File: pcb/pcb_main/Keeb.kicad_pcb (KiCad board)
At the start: 2 copper layers, 97.6 x 69.7 mm, 91 parts, among them J1 TRRS_SJ1-42514, Q1 PZT3906, SW1 SW_RST, SW2 SW_SPDT, U1 ATMEGA32U4, U2 SN74HC138D‎, U3 SN74HC251, U4 MCP73833, U5 LM8364-2.2, U6 LTC3525-5, X1 XTAL_GND

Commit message: Completed first revision of module1, started on module 2
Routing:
- net GND: track 93.7 -> 129.4 mm, vias 45 -> 35
- removed copper zone on F.Cu, net GND

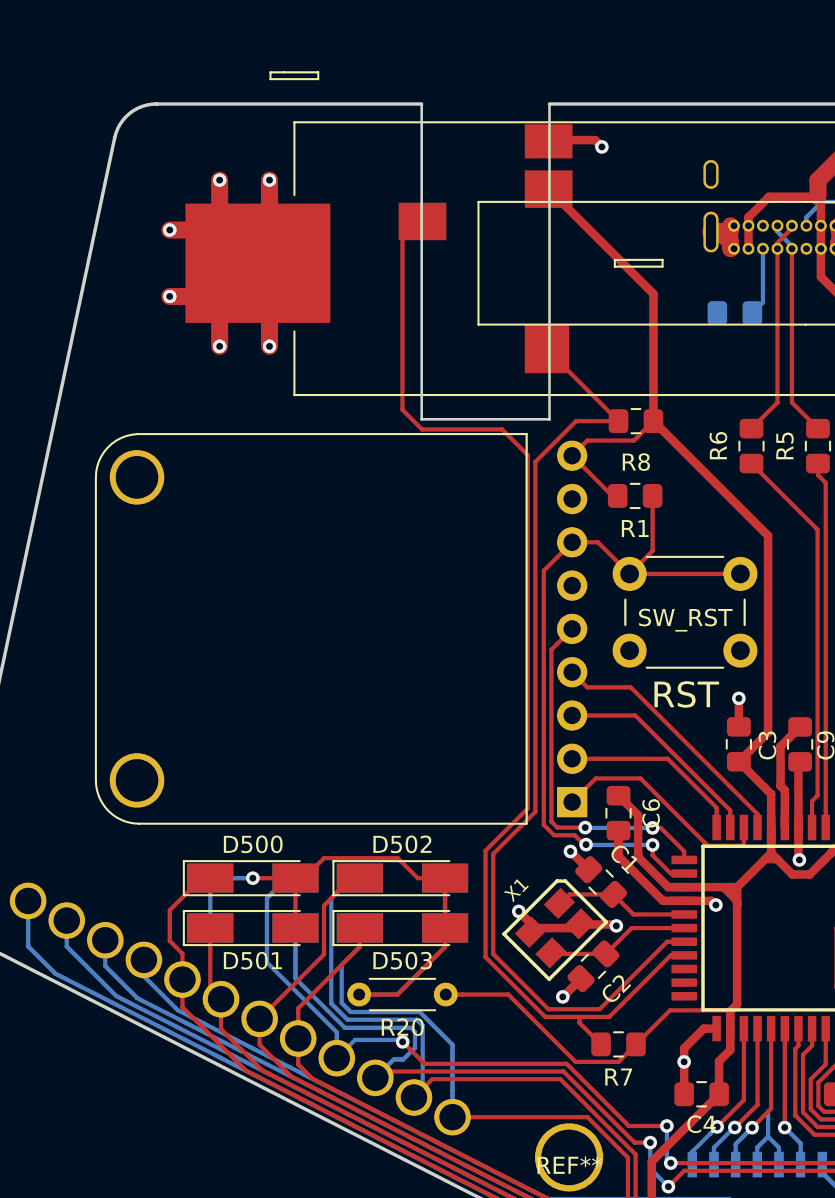
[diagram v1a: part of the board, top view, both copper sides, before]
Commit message: Rev 1 of module 2 & updated all-in-one cad drawing
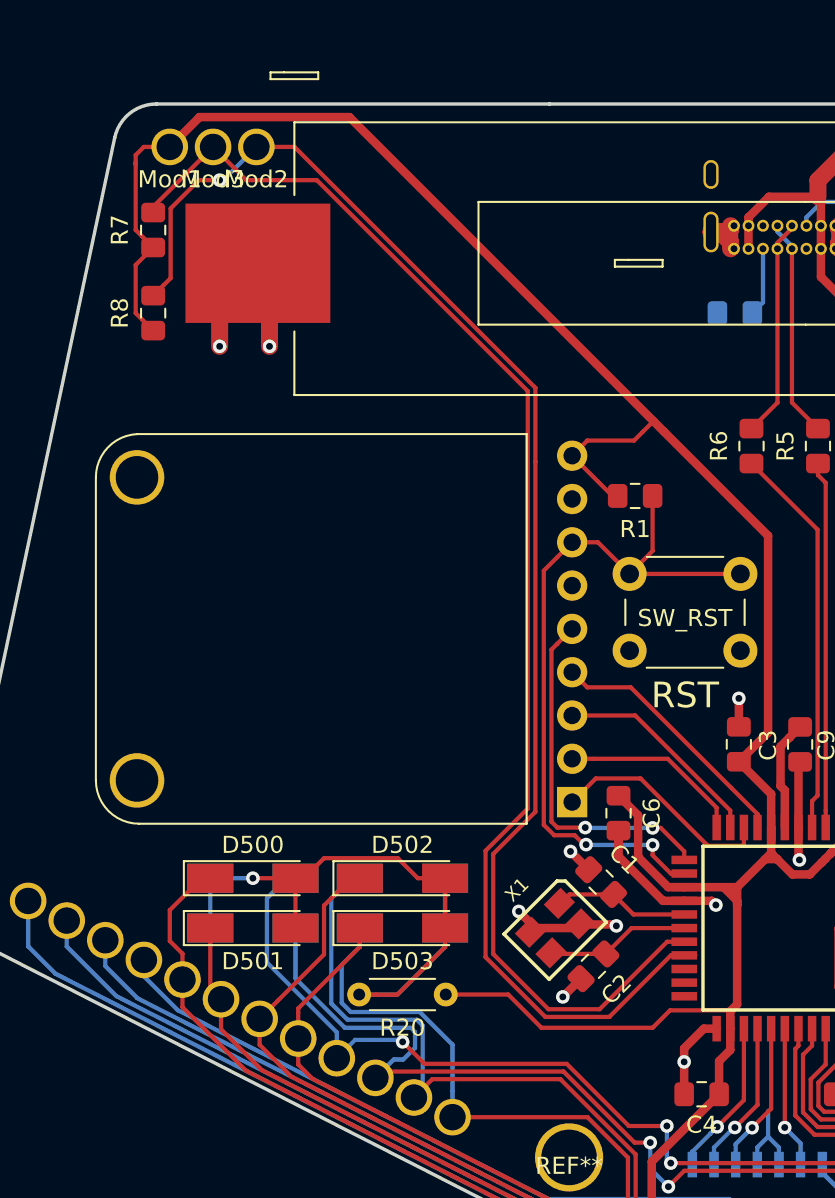
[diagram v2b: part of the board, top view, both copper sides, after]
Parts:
- removed J1: TRRS_SJ1-42514, SVastaCustomParts:3.5mm_Cut_out
- added Mod1: Conn_01x01_Male, SVastaCustomParts:Mill-Max_Pin_Socket_7305-0-15-15-47-27-10-0, F.Cu at (385.5, 162.0)
- added Mod2: Conn_01x01_Male, SVastaCustomParts:Mill-Max_Pin_Socket_7305-0-15-15-47-27-10-0, F.Cu at (390.5, 162.0)
- added Mod3: Conn_01x01_Male, SVastaCustomParts:Mill-Max_Pin_Socket_7305-0-15-15-47-27-10-0, F.Cu at (388.0, 162.0)
- moved R7 55.0 mm to (384.5, 166.9), turned to 270 degrees
- moved R8 29.0 mm to (384.5, 171.8), turned to 270 degrees
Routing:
- net VCC: track 213.7 -> 247.1 mm
- net SCL: track 55.1 -> 82.7 mm, vias 0 -> 1
- net GND: track 129.4 -> 113.4 mm, vias 35 -> 30
- net SDA: track 67.9 -> 79.2 mm
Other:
- outline, holes or cut-outs redrawn

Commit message: Updated connection method on main pcb
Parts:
- removed ColL0, ColL1, ColL2, ColL3, ColL4, ColL5, ColL6, ColL7, ColR0, ColR1, ColR2, ColR3, ColR4, ColR5, ColR6, ColR7, Mod1, Mod2, Mod3, Row0, Row1, Row2, Row3, Row4, Row5, Row6, Row7: Conn_01x01_Male, SVastaCustomParts:Mill-Max_Pin_Socket_7305-0-15-15-47-27-10-0
- removed REF** (x2): MountingHole_Imperial4-40_FreeFit, SVastaCustomParts:MountingHole_Imperial4-40_FreeFit
- added J101: Conn_02x10_Counter_Clockwise, SVastaCustomParts:Backplane_Connector_Hirose_PCN_20pos_Plug, F.Cu at (448.8, 206.9)
- added J102: Conn_02x10_Counter_Clockwise, SVastaCustomParts:Backplane_Connector_Hirose_PCN_20pos_Plug, F.Cu at (394.2, 206.9)
- D500, D501, D502, D503: footprint SVastaCustomParts:D_MiniMELF_Handsoldering_Shorter_Pads -> Diode_SMD:D_0805_2012Metric_Pad1.15x1.40mm_HandSolder; moved to B.Cu
- D504, D505, D506, D507: footprint SVastaCustomParts:D_MiniMELF_Handsoldering_Shorter_Pads -> Diode_SMD:D_0805_2012Metric_Pad1.15x1.40mm_HandSolder
- R20: footprint Resistor_THT:R_Axial_DIN0204_L3.6mm_D1.6mm_P5.08mm_Horizontal -> Resistor_SMD:R_0805_2012Metric_Pad1.15x1.40mm_HandSolder
- SW2: footprint SVastaCustomParts:400BWMSP1R2BLKSM6QE‎_rocker_switch -> SVastaCustomParts:SW_Slide_C&K_JS102011SAQN
- U3: moved to B.Cu
- moved R20 32.6 mm to (378.6, 186.4), turned to 270 degrees
- moved R7 25.1 mm to (378.6, 191.3)
- moved R8 25.1 mm to (378.6, 196.1), turned to 90 degrees
- moved D507 16.0 mm to (389.4, 195.2), turned to 270 degrees
- moved D505 13.0 mm to (393.3, 195.2), turned to 270 degrees
- moved D503 12.8 mm to (397.2, 195.2), turned to 270 degrees
- moved D500 11.8 mm to (401.1, 200.0), turned to 270 degrees
- moved D506 10.9 mm to (389.4, 200.0), turned to 270 degrees
- moved D501 10.4 mm to (397.2, 200.0), turned to 270 degrees
- moved D502 9.94 mm to (401.1, 195.2), turned to 270 degrees
- moved U3 6.78 mm to (445.9, 201.0), turned to 90 degrees
- moved D504 5.69 mm to (393.3, 200.0), turned to 270 degrees
- moved U2 4.97 mm to (421.5, 219.5)
- moved SW2 0.97 mm to (440.1, 164.0), turned to 0 degrees
- moved C10 0.27 mm to (460.5, 183.2)
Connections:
- SW2 pad 1: /BMS/5Vbat -> GND
- SW2 pad 3: GND -> /BMS/5Vbat
- U1 pad 29: ColSelectA -> ColValue
- U1 pad 30: ColSelectB -> ColSelectA
- U1 pad 31: ColSelectC -> ColSelectB
- U1 pad 32: ColValue -> ColEnable
- U1 pad 36: ColEnable -> ColSelectC
- U2 pad 10: /Row5 -> /Row2
- U2 pad 11: /Row4 -> /Row3
- U2 pad 12: /Row3 -> /Row4
- U2 pad 13: /Row2 -> /Row7
- U2 pad 14: /Row1 -> /Row6
- U2 pad 15: /Row0 -> /Row5
- U2 pad 7: /Row7 -> /Row0
- U2 pad 9: /Row6 -> /Row1
- U3 pad 15: /Col2 -> /Col3
- U3 pad 2: /Col1 -> /Col2
- U3 pad 3: /Col3 -> /Col1
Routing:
- net SDA: track 79.2 -> 156.3 mm
- net SCL: track 82.7 -> 150.5 mm
- net /Col7: track 79.1 -> 116.5 mm
- net Net-(D500-Pad2): track 41.0 -> 76.9 mm, vias 1 -> 4
- net /Row6: track 42.4 -> 72.0 mm, vias 0 -> 3
- net /Row5: track 47.4 -> 76.8 mm, vias 0 -> 3
- net /Row7: track 43.2 -> 70.4 mm, vias 0 -> 1
- net /Col5: track 88.9 -> 112.3 mm, vias 3 -> 0
- net /Row3: track 43.4 -> 66.3 mm, vias 0 -> 2
- net /Row0: track 48.9 -> 70.3 mm, vias 0 -> 2
- net /Row1: track 46.3 -> 67.1 mm, vias 0 -> 2
- net /Col6: track 87.0 -> 107.2 mm, vias 1 -> 0
- net /Row2: track 48.2 -> 66.8 mm, vias 0 -> 2
- net /Col0: track 99.2 -> 81.9 mm, vias 0 -> 2
- net /Row4: track 52.8 -> 69.1 mm, vias 0 -> 1
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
